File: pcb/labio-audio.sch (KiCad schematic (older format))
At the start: 31 parts, among them J701 JACK_TRRS_6PINS, P701 CONN_01X04, P702 CONN_01X04, P703 CONN_01X04, P704 CONN_01X02, SW701 DIP_SWITCH_X04, SW702 DIP_SWITCH_X04, U701 SPU0410HR5H, U702 WM8731

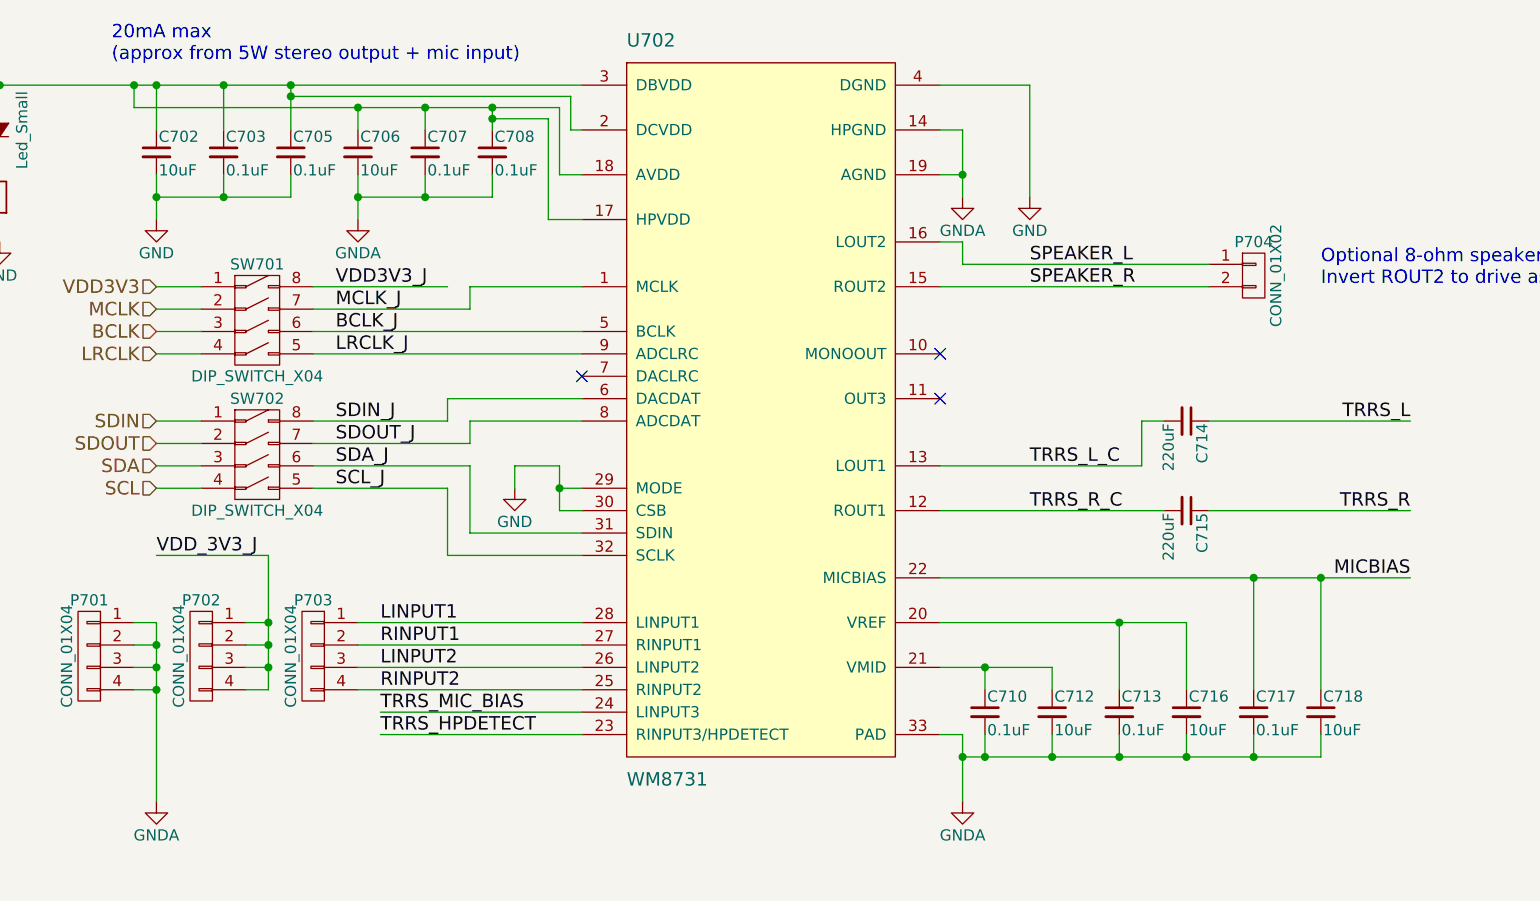
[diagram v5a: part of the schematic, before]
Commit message: floorplan on 150x85mm board, use al caps for motors
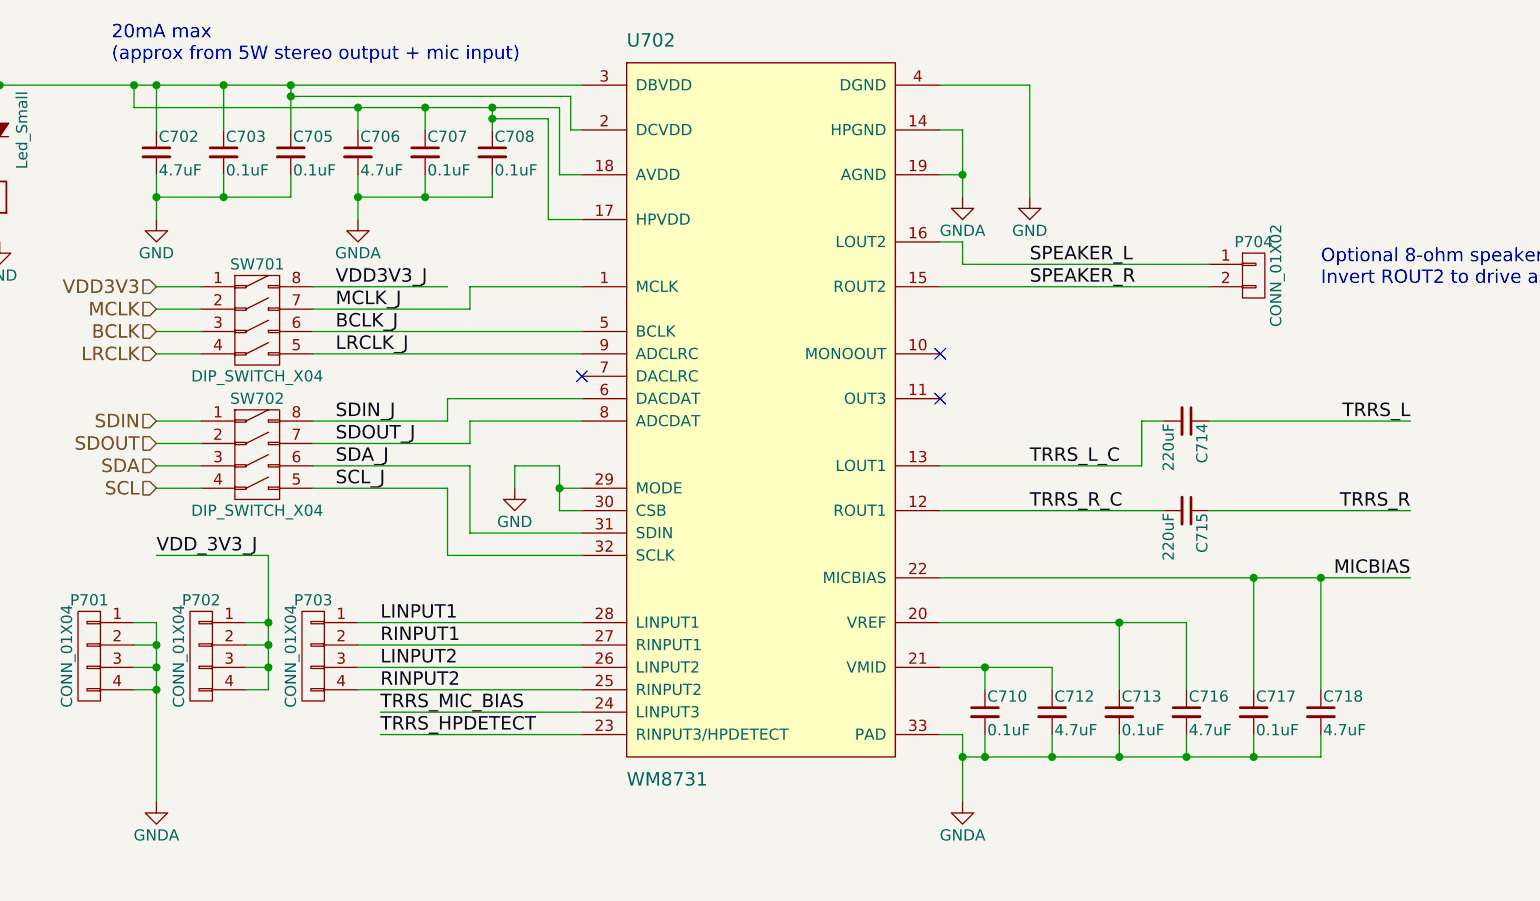
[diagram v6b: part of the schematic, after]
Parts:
- C702, C706, C712, C716, C718: value 10uF -> 4.7uF; footprint Capacitors_Tantalum_SMD:TantalC_SizeA_EIA-3216_Wave -> Capacitors_SMD:C_0603
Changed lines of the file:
@@
 $EndComp
 $Comp
-L GNDA #PWR033
+L GNDA #PWR034
 U 1 1 574CC7CB
 P 7000 4200
-F 0 "#PWR033" H 7000 3950 50  0001 C CNN
+F 0 "#PWR034" H 7000 3950 50  0001 C CNN
 F 1 "GNDA" H 7000 4050 50  0000 C CNN
 F 2 "" H 7000 4200 50  0000 C CNN
@@
 $EndComp
 $Comp
-L GNDA #PWR034
+L GNDA #PWR035
 U 1 1 574CC7ED
 P 7000 1500
-F 0 "#PWR034" H 7000 1250 50  0001 C CNN
+F 0 "#PWR035" H 7000 1250 50  0001 C CNN
 F 1 "GNDA" H 7000 1350 50  0000 C CNN
 F 2 "" H 7000 1500 50  0000 C CNN
@@
 Connection ~ 7000 1400
 $Comp
-L GND #PWR035
+L GND #PWR036
 U 1 1 574CC80B
 P 7300 1500
-F 0 "#PWR035" H 7300 1250 50  0001 C CNN
+F 0 "#PWR036" H 7300 1250 50  0001 C CNN
 F 1 "GND" H 7300 1350 50  0000 C CNN
 F 2 "" H 7300 1500 50  0000 C CNN
@@
 	7300 1000 6900 1000
 $Comp
-L GNDA #PWR036
+L GNDA #PWR037
 U 1 1 574CC826
 P 4300 1600
-F 0 "#PWR036" H 4300 1350 50  0001 C CNN
+F 0 "#PWR037" H 4300 1350 50  0001 C CNN
 F 1 "GNDA" H 4300 1450 50  0000 C CNN
 F 2 "" H 4300 1600 50  0000 C CNN
@@
 $EndComp
 $Comp
-L GND #PWR037
+L GND #PWR038
 U 1 1 574CC834
 P 3400 1600
-F 0 "#PWR037" H 3400 1350 50  0001 C CNN
+F 0 "#PWR038" H 3400 1350 50  0001 C CNN
 F 1 "GND" H 3400 1450 50  0000 C CNN
 F 2 "" H 3400 1600 50  0000 C CNN
@@
 P 3400 1300
 F 0 "C702" H 3410 1370 50  0000 L CNN
-F 1 "10uF" H 3410 1220 50  0000 L CNN
-F 2 "Capacitors_Tantalum_SMD:TantalC_SizeA_EIA-3216_Wave" H 3400 1300 50  0001 C CNN
+F 1 "4.7uF" H 3410 1220 50  0000 L CNN
+F 2 "Capacitors_SMD:C_0603" H 3400 1300 50  0001 C CNN
 F 3 "" H 3400 1300 50  0000 C CNN
 	1    3400 1300
@@
 P 4300 1300
 F 0 "C706" H 4310 1370 50  0000 L CNN
-F 1 "10uF" H 4310 1220 50  0000 L CNN
-F 2 "Capacitors_Tantalum_SMD:TantalC_SizeA_EIA-3216_Wave" H 4300 1300 50  0001 C CNN
+F 1 "4.7uF" H 4310 1220 50  0000 L CNN
+F 2 "Capacitors_SMD:C_0603" H 4300 1300 50  0001 C CNN
 F 3 "" H 4300 1300 50  0000 C CNN
 	1    4300 1300
@@
 	7000 3900 6900 3900
 $Comp
-L GNDA #PWR038
+L GNDA #PWR039
 U 1 1 574CD08C
 P 7900 5700
-F 0 "#PWR038" H 7900 5450 50  0001 C CNN
+F 0 "#PWR039" H 7900 5450 50  0001 C CNN
 F 1 "GNDA" H 7900 5550 50  0000 C CNN
 F 2 "" H 7900 5700 50  0000 C CNN
@@
 P 7400 3800
 F 0 "C712" H 7410 3870 50  0000 L CNN
-F 1 "10uF" H 7410 3720 50  0000 L CNN
-F 2 "Capacitors_Tantalum_SMD:TantalC_SizeA_EIA-3216_Wave" H 7400 3800 50  0001 C CNN
+F 1 "4.7uF" H 7410 3720 50  0000 L CNN
+F 2 "Capacitors_SMD:C_0603" H 7400 3800 50  0001 C CNN
 F 3 "" H 7400 3800 50  0000 C CNN
 	1    7400 3800
@@
 P 8000 3800
 F 0 "C716" H 8010 3870 50  0000 L CNN
-F 1 "10uF" H 8010 3720 50  0000 L CNN
-F 2 "Capacitors_Tantalum_SMD:TantalC_SizeA_EIA-3216_Wave" H 8000 3800 50  0001 C CNN
+F 1 "4.7uF" H 8010 3720 50  0000 L CNN
+F 2 "Capacitors_SMD:C_0603" H 8000 3800 50  0001 C CNN
 F 3 "" H 8000 3800 50  0000 C CNN
 	1    8000 3800
@@
 P 8600 3800
 F 0 "C718" H 8610 3870 50  0000 L CNN
-F 1 "10uF" H 8610 3720 50  0000 L CNN
-F 2 "Capacitors_Tantalum_SMD:TantalC_SizeA_EIA-3216_Wave" H 8600 3800 50  0001 C CNN
+F 1 "4.7uF" H 8610 3720 50  0000 L CNN
+F 2 "Capacitors_SMD:C_0603" H 8600 3800 50  0001 C CNN
 F 3 "" H 8600 3800 50  0000 C CNN
 	1    8600 3800
@@
 $EndComp
 $Comp
-L GNDA #PWR039
+L GNDA #PWR040
 U 1 1 574CE179
 P 3400 4200
-F 0 "#PWR039" H 3400 3950 50  0001 C CNN
+F 0 "#PWR040" H 3400 3950 50  0001 C CNN
 F 1 "GNDA" H 3400 4050 50  0000 C CNN
 F 2 "" H 3400 4200 50  0000 C CNN
@@
 $EndComp
 $Comp
-L GNDA #PWR040
+L GNDA #PWR041
 U 1 1 574D7F95
 P 3000 6000
-F 0 "#PWR040" H 3000 5750 50  0001 C CNN
+F 0 "#PWR041" H 3000 5750 50  0001 C CNN
 F 1 "GNDA" H 3000 5850 50  0000 C CNN
 F 2 "" H 3000 6000 50  0000 C CNN
@@
 	4800 2500 5300 2500
 $Comp
-L GND #PWR041
+L GND #PWR042
 U 1 1 574D9E5B
 P 5000 2800
-F 0 "#PWR041" H 5000 2550 50  0001 C CNN
+F 0 "#PWR042" H 5000 2550 50  0001 C CNN
 F 1 "GND" H 5000 2650 50  0000 C CNN
 F 2 "" H 5000 2800 50  0000 C CNN
@@
 Connection ~ 7000 5600
 $Comp
-L GNDA #PWR042
+L GNDA #PWR043
 U 1 1 575C906D
 P 6600 6100
-F 0 "#PWR042" H 6600 5850 50  0001 C CNN
+F 0 "#PWR043" H 6600 5850 50  0001 C CNN
 F 1 "GNDA" H 6600 5950 50  0000 C CNN
 F 2 "" H 6600 6100 50  0000 C CNN
@@
 $EndComp
 $Comp
-L GND #PWR043
+L GND #PWR044
 U 1 1 576D6E7D
 P 2700 1700
-F 0 "#PWR043" H 2700 1450 50  0001 C CNN
+F 0 "#PWR044" H 2700 1450 50  0001 C CNN
 F 1 "GND" H 2700 1550 50  0000 C CNN
 F 2 "" H 2700 1700 50  0000 C CNN

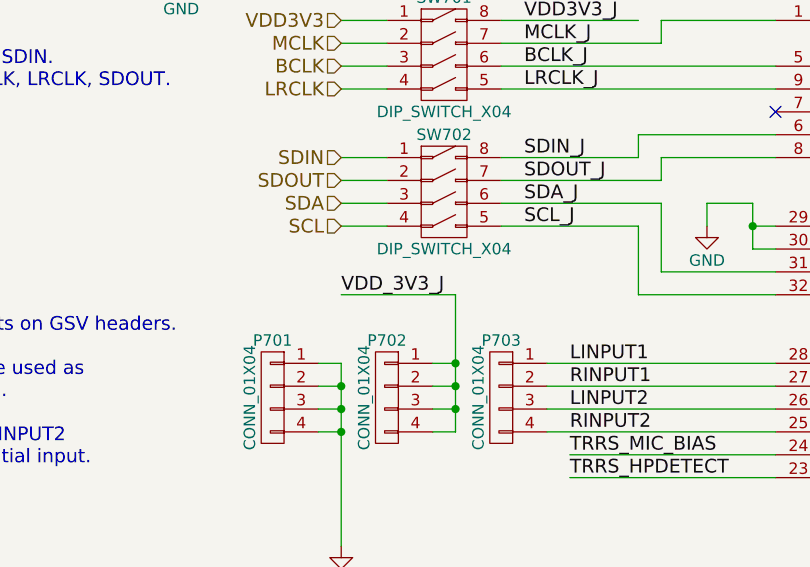
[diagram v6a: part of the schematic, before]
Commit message: first pass routing, fixed audio header 3v3 net
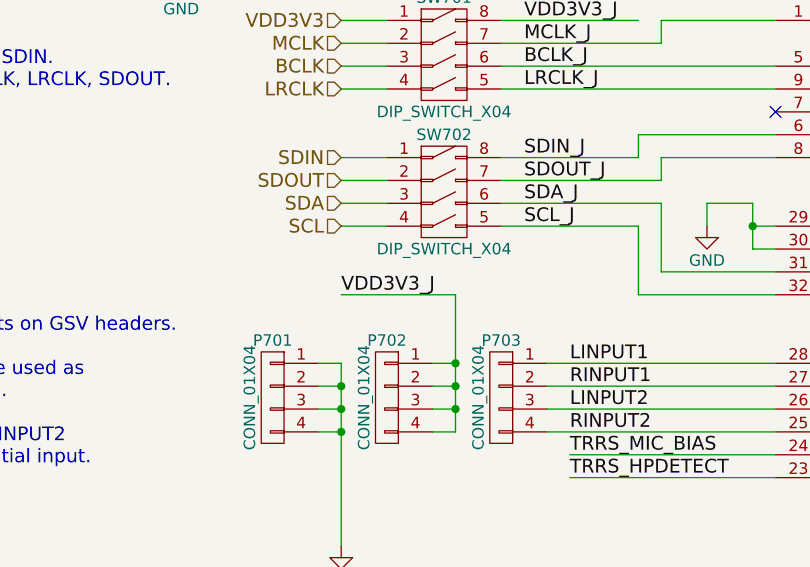
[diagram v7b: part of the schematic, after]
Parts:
- C702, C706, C712, C716, C718: footprint Capacitors_SMD:C_0603 -> Capacitors_SMD:C_0805
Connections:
- net VDD_3V3_J is gone; now on net VDD3V3_J: P702.1 (P1), P702.2 (P2), P702.3 (P3), P702.4 (P4)
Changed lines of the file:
@@
 F 0 "C702" H 3410 1370 50  0000 L CNN
 F 1 "4.7uF" H 3410 1220 50  0000 L CNN
-F 2 "Capacitors_SMD:C_0603" H 3400 1300 50  0001 C CNN
+F 2 "Capacitors_SMD:C_0805" H 3400 1300 50  0001 C CNN
 F 3 "" H 3400 1300 50  0000 C CNN
 	1    3400 1300
@@
 F 0 "C706" H 4310 1370 50  0000 L CNN
 F 1 "4.7uF" H 4310 1220 50  0000 L CNN
-F 2 "Capacitors_SMD:C_0603" H 4300 1300 50  0001 C CNN
+F 2 "Capacitors_SMD:C_0805" H 4300 1300 50  0001 C CNN
 F 3 "" H 4300 1300 50  0000 C CNN
 	1    4300 1300
@@
 F 0 "C712" H 7410 3870 50  0000 L CNN
 F 1 "4.7uF" H 7410 3720 50  0000 L CNN
-F 2 "Capacitors_SMD:C_0603" H 7400 3800 50  0001 C CNN
+F 2 "Capacitors_SMD:C_0805" H 7400 3800 50  0001 C CNN
 F 3 "" H 7400 3800 50  0000 C CNN
 	1    7400 3800
@@
 F 0 "C716" H 8010 3870 50  0000 L CNN
 F 1 "4.7uF" H 8010 3720 50  0000 L CNN
-F 2 "Capacitors_SMD:C_0603" H 8000 3800 50  0001 C CNN
+F 2 "Capacitors_SMD:C_0805" H 8000 3800 50  0001 C CNN
 F 3 "" H 8000 3800 50  0000 C CNN
 	1    8000 3800
@@
 F 0 "C718" H 8610 3870 50  0000 L CNN
 F 1 "4.7uF" H 8610 3720 50  0000 L CNN
-F 2 "Capacitors_SMD:C_0603" H 8600 3800 50  0001 C CNN
+F 2 "Capacitors_SMD:C_0805" H 8600 3800 50  0001 C CNN
 F 3 "" H 8600 3800 50  0000 C CNN
 	1    8600 3800
@@
 VDD3V3_J
 Text Label 3400 3100 0    60   ~ 0
-VDD_3V3_J
+VDD3V3_J
 $Comp
 L DIP_SWITCH_X04 SW701
